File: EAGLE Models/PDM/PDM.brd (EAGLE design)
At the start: 160 x 100 mm, 19 parts

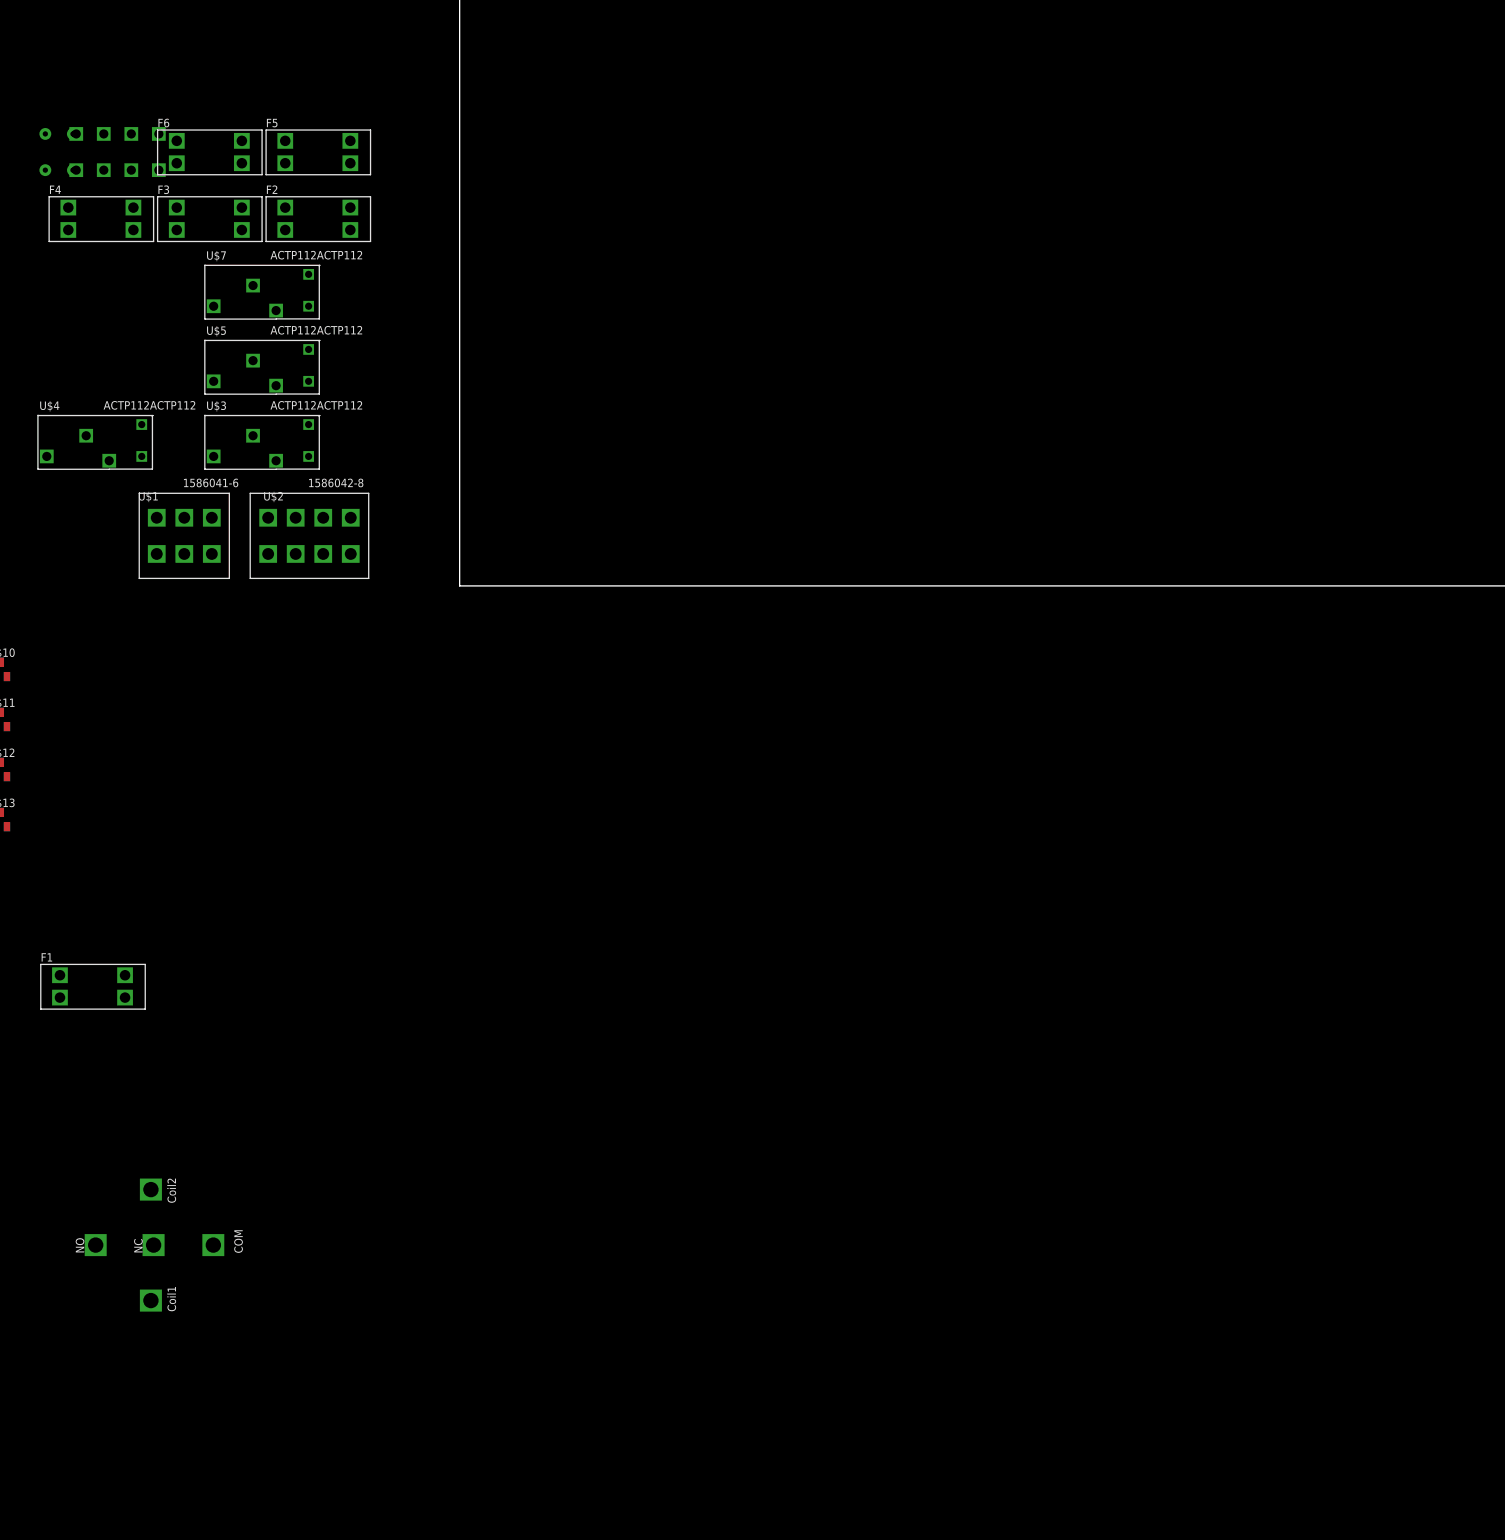
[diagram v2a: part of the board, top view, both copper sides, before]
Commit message: Updated pads on connectors, added another fuse on the board, modified schematic
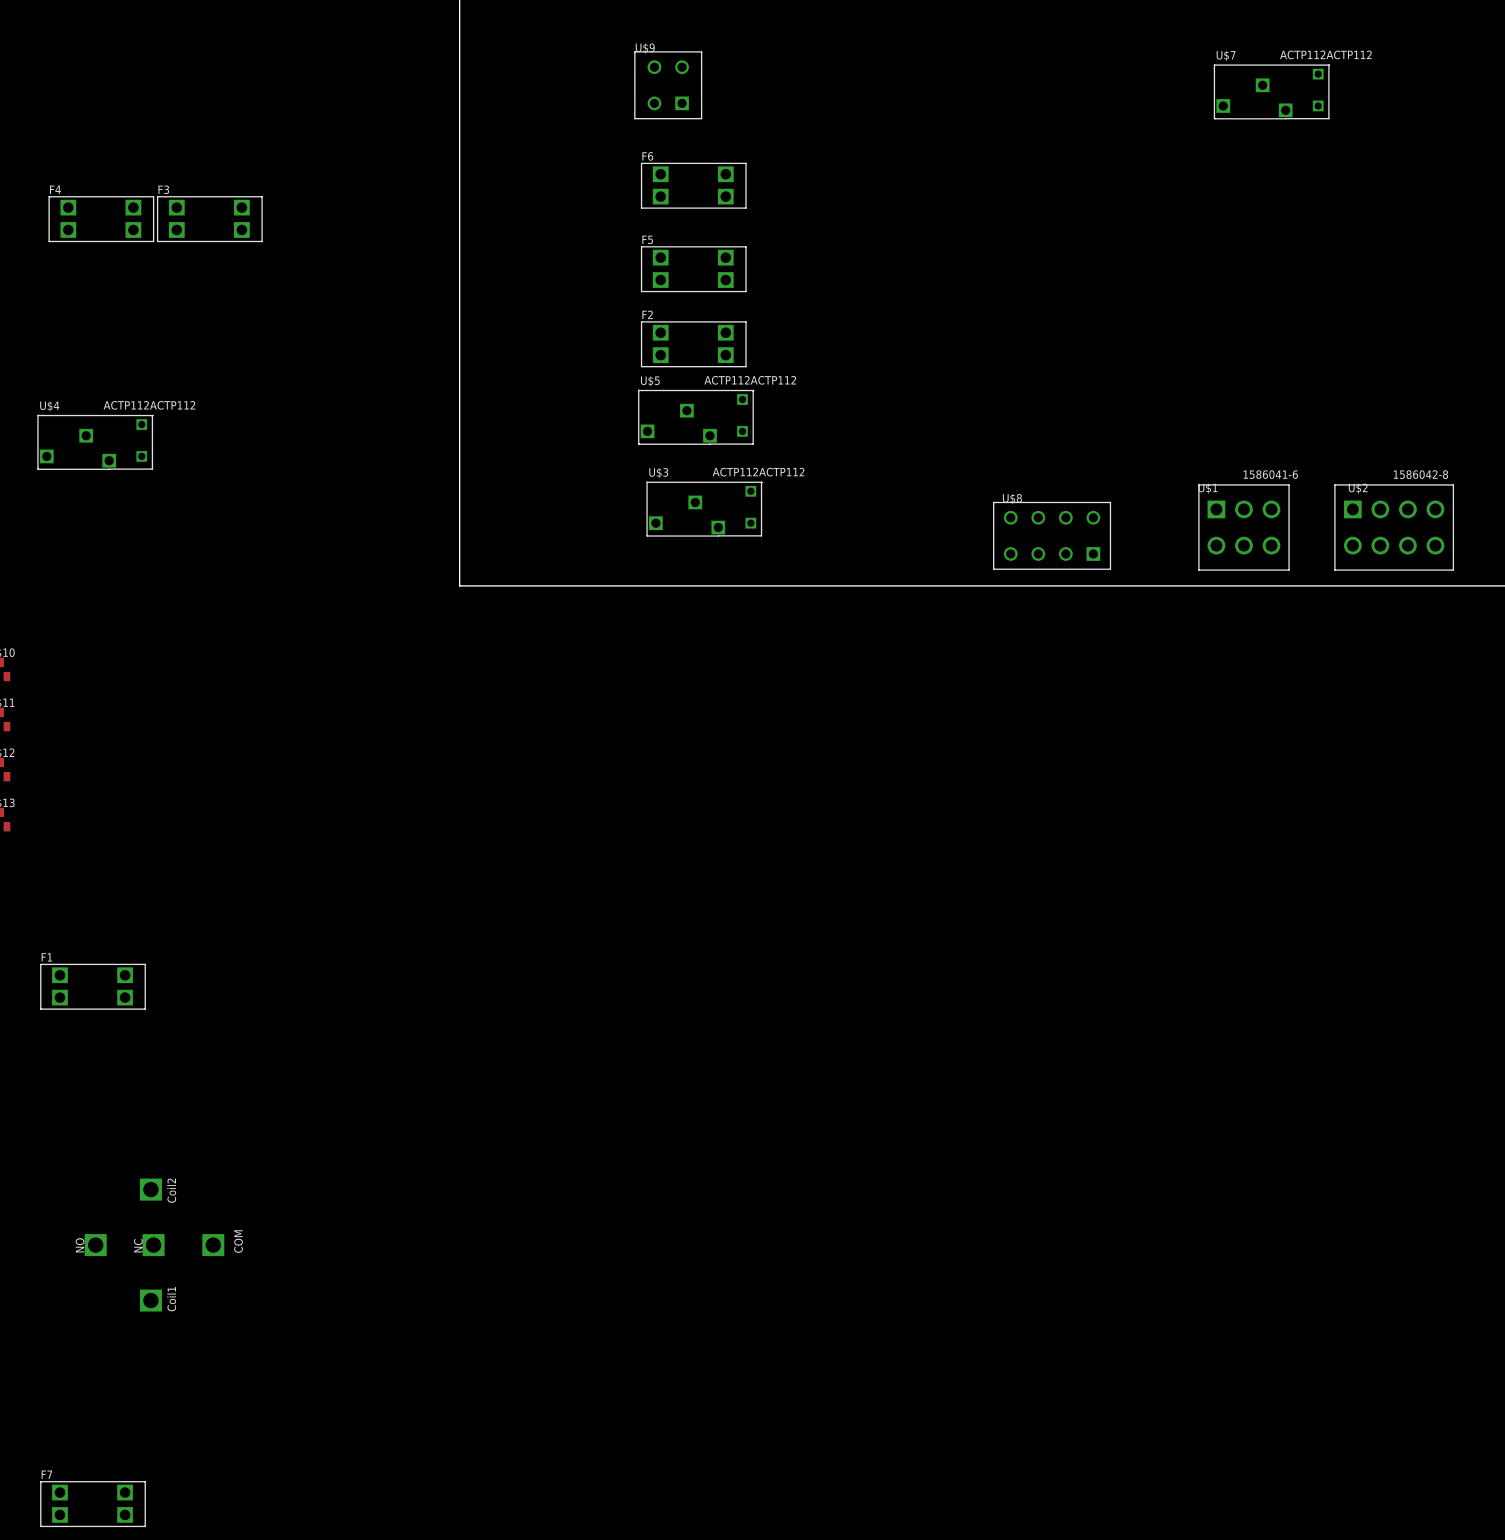
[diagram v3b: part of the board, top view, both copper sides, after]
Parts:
- added F7: 3568, Keystone:3568
- moved U$2 165.1 mm to (142.2, 8.89)
- moved U$1 161.3 mm to (119.4, 8.89)
- moved U$7 156.7 mm to (125.7, 72.4)
- moved U$8 153.8 mm to (90.2, 7.62)
- moved U$9 93.3 mm to (31.8, 76.2)
- moved F6 73.8 mm to (35.6, 61.0)
- moved U$3 68.1 mm to (39.4, 8.89)
- moved U$5 66.5 mm to (38.1, 22.9)
- moved F2 60.2 mm to (35.6, 36.8)
- moved F5 59.9 mm to (35.6, 48.3)
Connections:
- removed net BAT_GND: U$9.3, U$9.4
- new net 12V_FUSED_ECU: F7.3, F7.4, U$2.2, U$2.4
- new net N$7: F7.1, F7.2
- net 12V_DAQ_OUT: no longer U$2.2, U$2.4
- net FAN: no longer U$8.8
- net GND: now also U$8.8, U$9.3, U$9.4

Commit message: Started board layout, changed details on molex package for connectors
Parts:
- moved F7 255.4 mm to (134.6, 30.5), turned to 270 degrees
- moved U$15 200.1 mm to (62.2, 67.3), turned to 270 degrees
- moved F3 192.2 mm to (152.4, 30.5), turned to 270 degrees
- moved F1 191.2 mm to (91.4, 61.0), turned to 270 degrees
- moved U$4 182.1 mm to (128.3, 33.0), turned to 90 degrees
- moved U$10 181.0 mm to (86.4, 78.7)
- moved U$13 161.3 mm to (74.9, 35.6)
- moved U$12 134.4 mm to (54.6, 22.9)
- moved U$11 128.1 mm to (50.8, 22.9)
- moved F4 122.6 mm to (64.8, 27.9)
- moved F6 112.2 mm to (143.5, 30.5), turned to 270 degrees
- moved F2 77.8 mm to (113.0, 29.2), turned to 270 degrees
- moved U$9 70.6 mm to (101.6, 66.0), turned to 180 degrees
- moved U$5 67.7 mm to (105.4, 30.5), turned to 90 degrees
- moved U$3 56.8 mm to (90.2, 34.3), turned to 90 degrees
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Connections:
- removed net N$7: F7.1, F7.2
- net 12V: now also F7.1, F7.2
- net FAN: now also U$8.2; no longer U$8.4
- net FUEL: now also U$8.3; no longer U$8.2
- net IGNITION: now also U$8.4; no longer U$8.3
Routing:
- added copper zone on layer 1, net GND
- added copper zone on layer 16, net GND
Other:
- board size 160 x 100 mm -> 158.8 x 108 mm

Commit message: updated board layout
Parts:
- moved U$10 28.7 mm to (106.7, 99.1)
- moved U$13 23.3 mm to (92.5, 50.8), turned to 270 degrees
- moved U$9 22.2 mm to (96.5, 87.6), turned to 270 degrees
- moved F7 21.1 mm to (152.3, 41.9)
- moved F3 21.0 mm to (134.8, 41.9)
- moved U$15 15.9 mm to (55.8, 81.8)
- moved U$5 12.7 mm to (105.8, 43.2)
- moved F2 12.7 mm to (113.0, 41.9)
- moved U$7 12.0 mm to (81.3, 74.9)
- moved F6 11.5 mm to (143.6, 42.0)
- moved U$4 11.4 mm to (128.3, 44.5)
- moved F1 11.2 mm to (95.3, 71.5), turned to 0 degrees
- moved U$1 10.7 mm to (111.3, 61.3)
- moved F5 7.41 mm to (54.6, 48.3)
- moved F4 6.75 mm to (68.0, 33.9), turned to 270 degrees
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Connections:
- net 12V_DAQ_OUT: now also U$2.2; no longer U$2.3
- net 12V_FUSED_ECU: now also U$2.3; no longer U$2.2
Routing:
- net RECTIFIER: track 0.00 -> 54.6 mm
- net IGNITION: track 0.00 -> 38.4 mm
- net 12V_FUSED_ECU: track 0.00 -> 29.9 mm
- net 12V_DAQ_OUT: track 0.00 -> 29.8 mm
- net FAN: track 0.00 -> 26.6 mm
- net FUEL: track 0.00 -> 26.5 mm
- net N$6: track 0.00 -> 10.4 mm
- net N$5: track 0.00 -> 9.30 mm
- net BAT_+12: track 0.00 -> 4.51 mm

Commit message: Updated Board Design
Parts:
- moved F1 30.5 mm to (64.8, 70.2)
- moved F2 30.5 mm to (82.5, 40.6)
- moved F3 30.5 mm to (104.4, 40.7)
- moved U$1 30.5 mm to (80.8, 60.0)
- moved U$10 30.5 mm to (76.2, 97.8)
- moved U$2 30.5 mm to (108.0, 11.4)
- moved U$3 30.5 mm to (59.7, 38.1)
- moved U$4 30.5 mm to (97.8, 43.2)
- moved U$5 30.5 mm to (75.3, 41.9)
- moved U$7 30.5 mm to (50.8, 73.7)
- moved F5 30.5 mm to (24.1, 47.0)
- moved U$12 30.5 mm to (24.1, 21.6)
- moved U$15 30.5 mm to (25.3, 80.5)
- moved U$11 30.5 mm to (20.3, 21.6)
- moved U$13 30.5 mm to (62.0, 49.5)
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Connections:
- net N$5 renamed IGN_12V
- net N$6 renamed FUEL_12V
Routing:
- net IGN_12V: track 9.30 -> 0.00 mm
- added copper zone on layer 1, net N$1
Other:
- board size 158.8 x 108 mm -> 130.5 x 103.6 mm

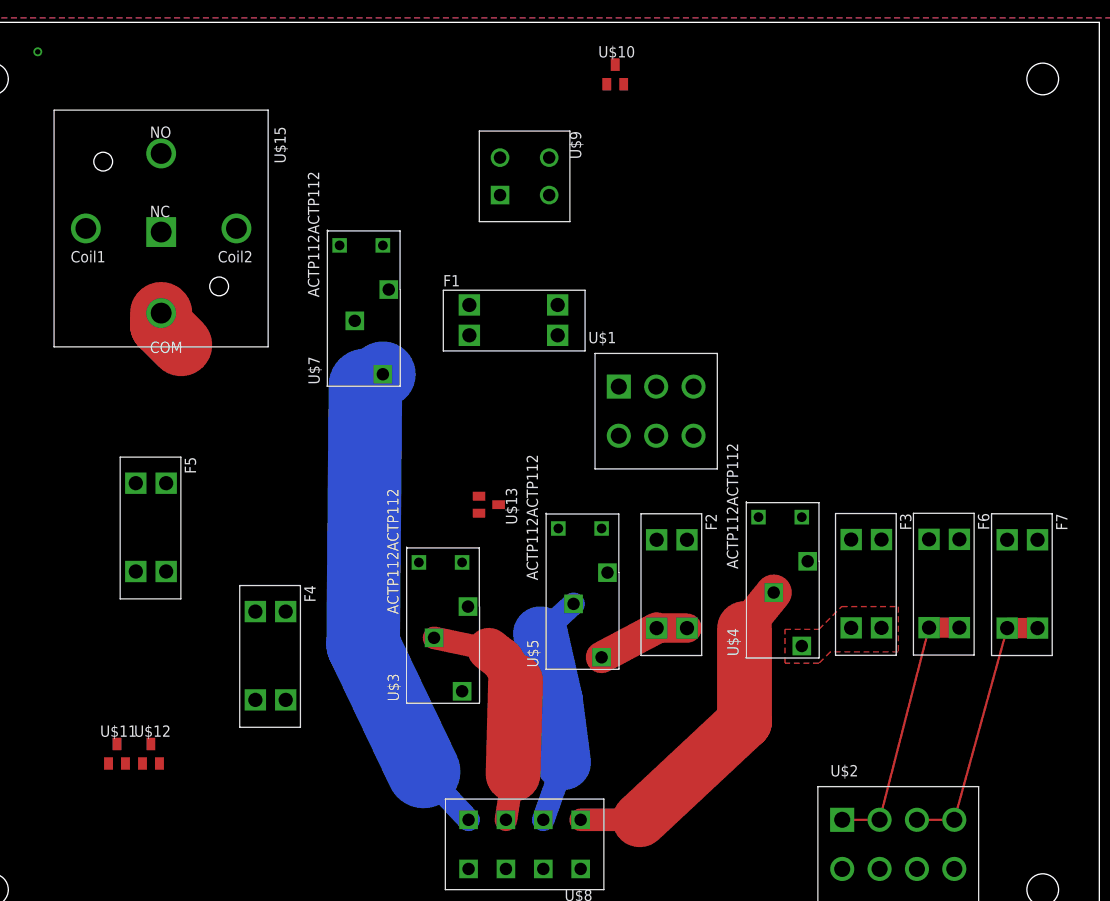
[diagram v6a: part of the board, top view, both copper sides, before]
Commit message: Updated board design, need to connect diodes and gnd plane
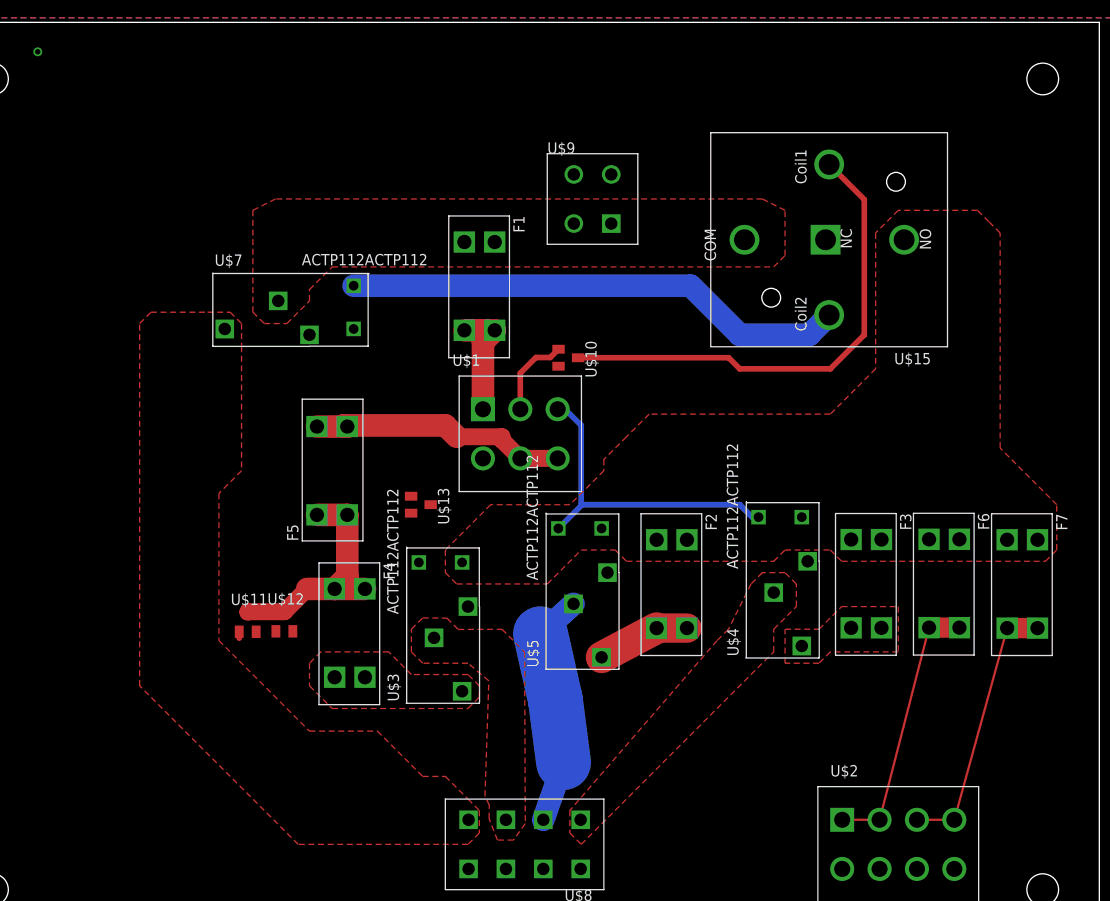
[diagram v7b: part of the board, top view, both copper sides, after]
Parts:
- moved U$15 74.9 mm to (100.2, 79.2), turned to 180 degrees
- moved U$10 32.2 mm to (70.9, 66.0), turned to 270 degrees
- moved F5 21.3 mm to (44.5, 53.3), turned to 90 degrees
- moved U$12 21.1 mm to (39.1, 36.4)
- moved U$11 20.8 mm to (35.0, 36.4)
- moved U$1 15.5 mm to (65.6, 57.5)
- moved U$7 10.2 mm to (41.9, 68.6), turned to 0 degrees
- moved F4 9.25 mm to (46.4, 35.1)
- moved U$9 8.03 mm to (73.7, 83.8), turned to 0 degrees
- moved U$13 7.62 mm to (54.4, 49.5)
- moved F1 5.39 mm to (61.0, 74.0), turned to 270 degrees
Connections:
- net N$3 renamed FAN_12V
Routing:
- net CHARGE_CUT_IN: track 0.00 -> 56.5 mm
- net MAIN_RELAY_IN: track 0.00 -> 54.9 mm
- net RECTIFIER: track 54.6 -> 0.00 mm
- net IGNITION: track 38.4 -> 0.00 mm
- net A24: track 0.00 -> 37.2 mm
- net 12V_SHIFT_OUT: track 0.00 -> 29.7 mm
- net FAN: track 26.6 -> 0.00 mm
- net 12V: track 0.00 -> 26.5 mm
- net BAT_+12_FUSED: track 0.00 -> 12.8 mm
- net KILL_SWT: track 0.00 -> 9.45 mm
- net BAT_+12: track 4.51 -> 0.00 mm
- net A23: track 0.00 -> 0.61 mm
- added copper zone on layer 1, net 12V
- added copper zone on layer 1, net BAT_+12
- added copper zone on layer 1, net FAN
- added copper zone on layer 1, net FAN_12V
- added copper zone on layer 1, net IGNITION
- added copper zone on layer 1, net RECTIFIER
